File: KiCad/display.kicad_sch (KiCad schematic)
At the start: 18 parts, among them J7 Conn_01x16_Female, Q3 Q_NMOS_DGS, U5 AP3012, U6 PCF8574

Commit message: -associated footprints to more specific components -added manufacturer and part series info to more specific components
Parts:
- C22, C23: value C -> 1u
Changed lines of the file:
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@@
       (effects (font (size 1.27 1.27)) (justify left))
     )
-    (property "Value" "C" (id 1) (at 153.67 148.5899 0)
+    (property "Value" "1u" (id 1) (at 153.67 148.5899 0)
       (effects (font (size 1.27 1.27)) (justify left))
     )
@@
       (effects (font (size 1.27 1.27)) (justify left))
     )
-    (property "Value" "C" (id 1) (at 93.98 147.3199 0)
+    (property "Value" "1u" (id 1) (at 93.98 147.3199 0)
       (effects (font (size 1.27 1.27)) (justify left))
     )

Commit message: -layout work
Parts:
- D4: value D_Schottky -> 30V 1A; footprint (none) -> Diode_SMD:D_SOD-323; MFG (none) -> Toshiba Semiconductor and Storage; MFG# (none) -> CUS10S30,H3F
- L5: value L -> 33u; footprint (none) -> Inductor_SMD:L_Taiyo-Yuden_NR-50xx; MFG (none) -> Taiyo Yuden; MFG# (none) -> NRS5030T330MMGJ
- Q3: value Q_NMOS_DGS -> 2N7002; footprint (none) -> Package_TO_SOT_SMD:SOT-323_SC-70; symbol Device:Q_NMOS_DGS -> Device:Q_NMOS_GSD; MFG (none) -> Nexperia USA Inc.; MFG# (none) -> 2N7002PW,115
- RV2: value R_Potentiometer_Trim -> TC33X_10k; footprint (none) -> Custom:trimmer_Bourns_tc33x; MFG (none) -> Bourns Inc.
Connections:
- net +3V3: no longer C22.1, L5.1, U5.5 (IN)
- net GND: now also Q3.2 (S); no longer Q3.3 (S)
- net LCD_BCKL_EN: now also Q3.1 (G); no longer Q3.2 (G)
- net at J7.16 (Pin_16): now also Q3.3 (D); no longer Q3.1 (D)
- new net +VDC: C22.1, L5.1, U5.5 (IN)
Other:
- moved on the sheet: C23

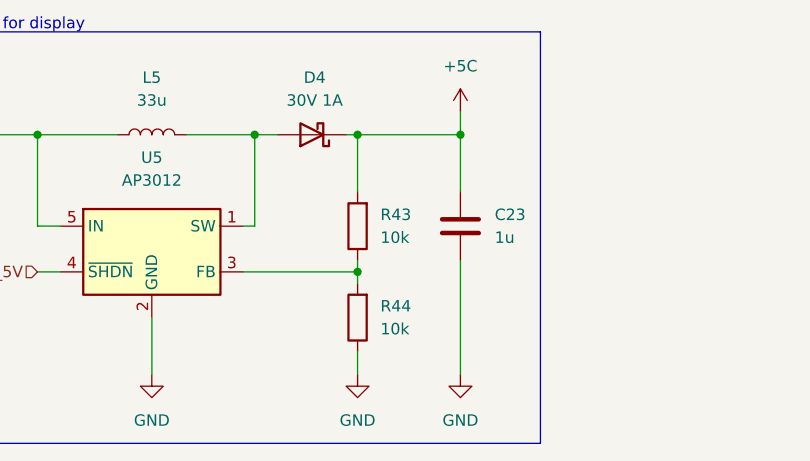
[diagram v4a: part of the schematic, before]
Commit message: -updated schematic component values, updated schematic PDF -added simple bass and treble control for the TF9879 amp
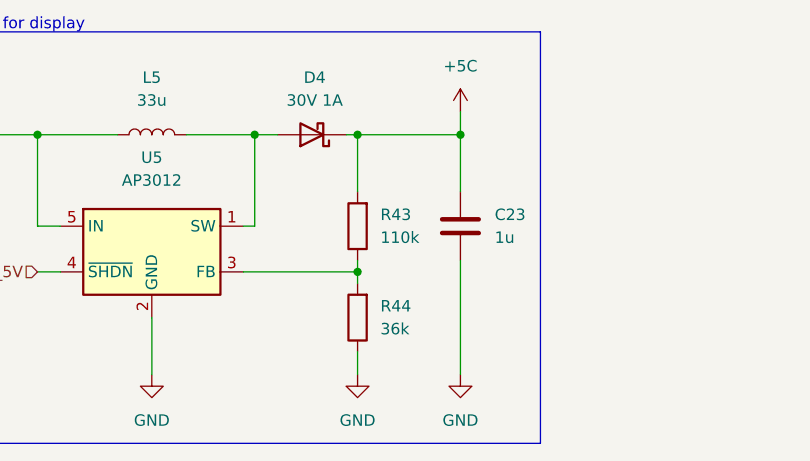
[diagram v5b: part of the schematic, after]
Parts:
- R43: value 10k -> 110k
- R44: value 10k -> 36k
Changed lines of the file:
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@@
       (effects (font (size 1.27 1.27)) (justify right))
     )
-    (property "Value" "10k" (id 1) (at 143.51 148.5899 0)
+    (property "Value" "110k" (id 1) (at 143.51 148.5899 0)
       (effects (font (size 1.27 1.27)) (justify right))
     )
@@
       (effects (font (size 1.27 1.27)) (justify right))
     )
-    (property "Value" "10k" (id 1) (at 143.51 158.7499 0)
-      (effects (font (size 1.27 1.27)) (justify right))
-    )
+    (property "Value" "36k" (id 1) (at 143.51 158.7499 0)
+      (effects (font (size 1.27 1.27)) (justify right))
+    )
